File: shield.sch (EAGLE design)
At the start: 40 parts, among them Q1 BSS138, Q2 BSS138, Q3 BSS138, Q4 BSS138, Q5 BSS138, Q6 BSS138, Q7 BSS138, Q8 BSS138

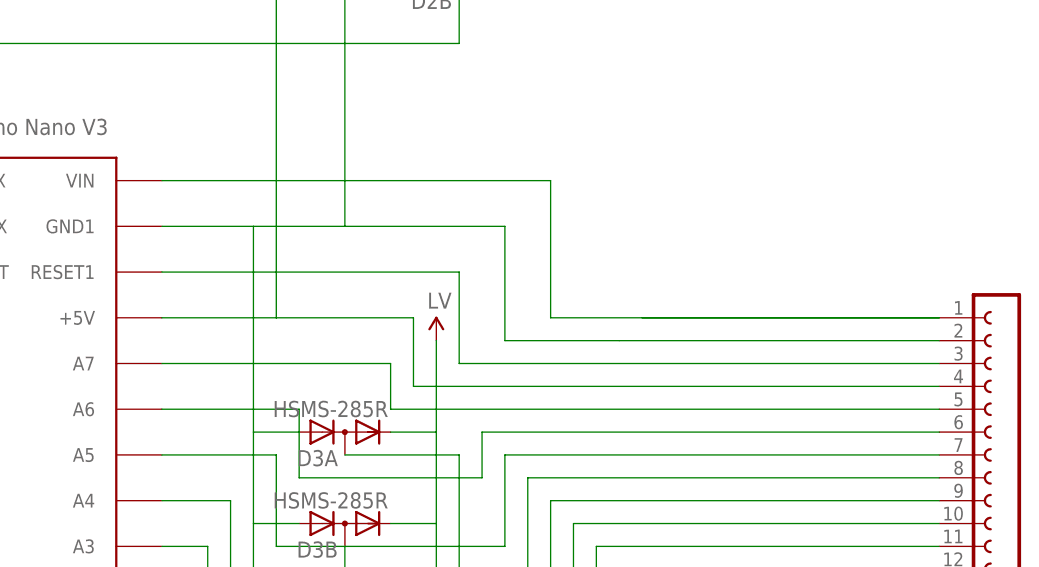
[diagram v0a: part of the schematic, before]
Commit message: fixing ground line
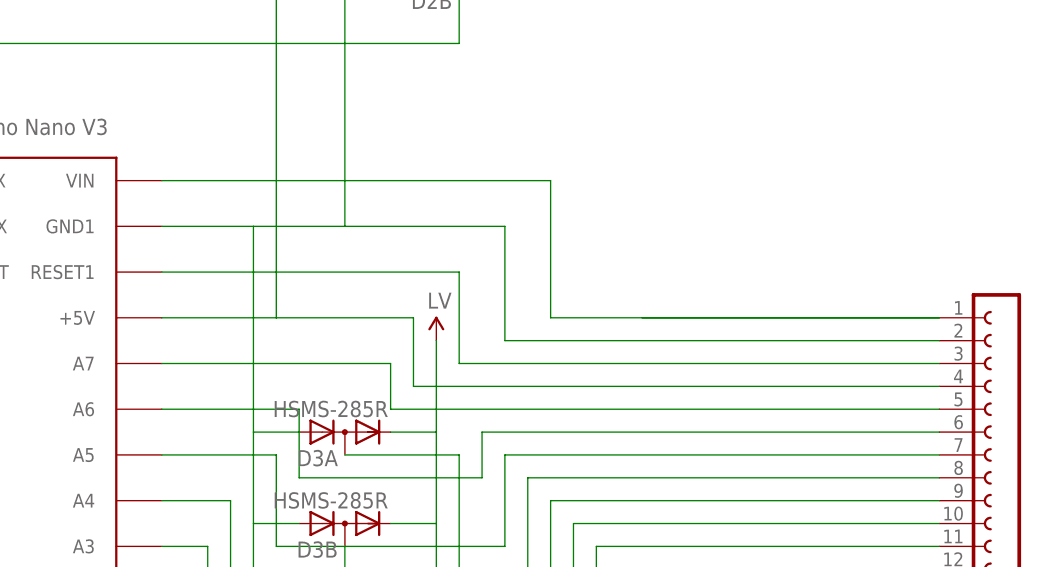
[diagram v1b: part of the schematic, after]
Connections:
- removed net N$15: SV2.2
- net N$1: now also SV2.2
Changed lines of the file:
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@@
 <net name="N$1" class="0">
 <segment>
-<pinref part="U$1" gate="G$1" pin="GND1"/>
-<wire x1="55.88" y1="78.74" x2="66.04" y2="78.74" width="0.1524" layer="91"/>
 <wire x1="66.04" y1="78.74" x2="76.2" y2="78.74" width="0.1524" layer="91"/>
 <wire x1="76.2" y1="78.74" x2="76.2" y2="106.68" width="0.1524" layer="91"/>
@@
 <wire x1="76.2" y1="78.74" x2="93.98" y2="78.74" width="0.1524" layer="91"/>
 <wire x1="93.98" y1="78.74" x2="93.98" y2="66.04" width="0.1524" layer="91"/>
-<wire x1="93.98" y1="66.04" x2="106.68" y2="66.04" width="0.1524" layer="91"/>
+<pinref part="U$1" gate="G$1" pin="GND1"/>
+<wire x1="66.04" y1="78.74" x2="55.88" y2="78.74" width="0.1524" layer="91"/>
+<pinref part="SV2" gate="G$1" pin="2"/>
+<wire x1="93.98" y1="66.04" x2="142.24" y2="66.04" width="0.1524" layer="91"/>
 </segment>
 </net>
@@
 </segment>
 </net>
-<net name="N$15" class="0">
-<segment>
-<pinref part="SV2" gate="G$1" pin="2"/>
-<wire x1="142.24" y1="66.04" x2="106.68" y2="66.04" width="0.1524" layer="91"/>
-</segment>
-</net>
